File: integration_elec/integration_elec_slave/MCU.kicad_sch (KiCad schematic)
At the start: 0 parts

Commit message: EM - Ajout des pages hiérarchiques pour le slave, next up : Master
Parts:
- added C1, C2, C3, C4, C5, C6, C7, C8, C9: 0.10uF, Capacitor_SMD:C_0805_2012Metric_Pad1.18x1.45mm_HandSolder, symbol Device:C_Small
- added C10: 4.7uF, Capacitor_SMD:C_0805_2012Metric_Pad1.18x1.45mm_HandSolder, symbol Device:C_Small
- added C11, C12: 10pF, Capacitor_SMD:C_0805_2012Metric_Pad1.18x1.45mm_HandSolder, symbol Device:C_Small
- added L1: FerritBead 600 OHM, Inductor_SMD:L_0805_2012Metric_Pad1.15x1.40mm_HandSolder, symbol Device:FerriteBead
- added R2, R3, R38: 10k, Resistor_SMD:R_0805_2012Metric_Pad1.20x1.40mm_HandSolder, symbol Device:R_US
- added R37: 120, Resistor_SMD:R_0805_2012Metric_Pad1.20x1.40mm_HandSolder, symbol Device:R_US
- added SW1: SW_Push, Button_Switch_SMD:SW_SPST_TL3342, symbol Switch:SW_Push
- added U1: STM32F446RETx, Package_QFP:LQFP-64_10x10mm_P0.5mm, symbol MCU_ST_STM32F4:STM32F446RETx
- added Y1: Crystal_16MHz, ab2_xtal:CSM-3X, symbol Device:Crystal
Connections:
- new net: C6.2, L1.2, U1.13 (VDDA)
- new net: C10.2, C9.2, U1.30 (VCAP_1)
- new net: R3.2, U1.34 (PB13)
- new net: C11.1, U1.5 (PH0), Y1.1
- new net: C12.1, U1.6 (PH1), Y1.2
- new net: R2.1, U1.60 (BOOT0)
- new net: R37.1, SW1.1
- new net +3V3: C1.1, C2.1, C3.1, C4.1, C5.1, C7.1, L1.1, R38.1, U1.1 (VBAT), U1.19 (VDD), U1.32 (VDD), U1.48 (VDD), U1.64 (VDD)
- new net DEBUG_NJTRST: U1.56 (PB4)
- new net DEBUG_RESET: C8.1, R38.2, SW1.2, U1.7 (NRST)
- new net DEBUG_SWCLK_TCK: U1.49 (PA14)
- new net DEBUG_SWDIO_TMS: U1.46 (PA13)
- new net DEBUG_SWO_TDI: U1.50 (PA15)
- new net DEBUG_SWO_TDO: U1.55 (PB3)
- new net DEBUG_UART_RX: U1.25 (PC5)
- new net DEBUG_UART_TX: U1.29 (PB10)
- new net GND: C1.2, C10.1, C11.2, C12.2, C2.2, C3.2, C4.2, C5.2, C6.1, C7.2, C8.2, C9.1, R2.2, R37.2, U1.12 (VSSA), U1.18 (VSS), U1.31 (VSS), U1.47 (VSS), U1.63 (VSS)
- new net RF.XBEE_LED: U1.24 (PC4)
- new net RF.XBEE_RQ: U1.41 (PA8)
- new net RF.XBEE_STATUS: U1.40 (PC9)
- new net RF.XBEE_UART_CTS: U1.44 (PA11)
- new net RF.XBEE_UART_IN: U1.42 (PA9)
- new net RF.XBEE_UART_OUT: U1.43 (PA10)
- new net RF.XBEE_UART_RTS: U1.45 (PA12)
- new net RF.XBEE_nReset: U1.51 (PC10)
- new net SD_SDIO_CLK: U1.28 (PB2)
- new net SD_SDIO_CMD: U1.54 (PD2)
- new net SD_SDIO_D0: U1.39 (PC8)
- new net SD_SDIO_D1: U1.26 (PB0)
- new net SD_SDIO_D2: U1.27 (PB1)
- new net SD_SDIO_D3: U1.52 (PC11)
- new net SD_SDIO_SW: U1.53 (PC12)
- new net USB_D+: U1.36 (PB15)
- new net USB_D-: U1.35 (PB14)
- new net USB_ID: U1.33 (PB12)
- new net USB_VBUS: R3.1
- no-connect marks 0 -> 5
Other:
- note added: "If the flash is blank, the bootloader will enable."
- note added: "RESET"
- note added: "Stabilization for the main regulator"

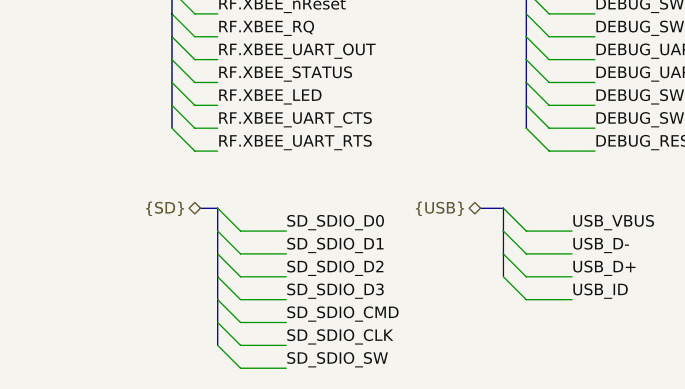
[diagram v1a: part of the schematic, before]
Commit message: EM - Avancement du slave et determination ADC pour LTF6800
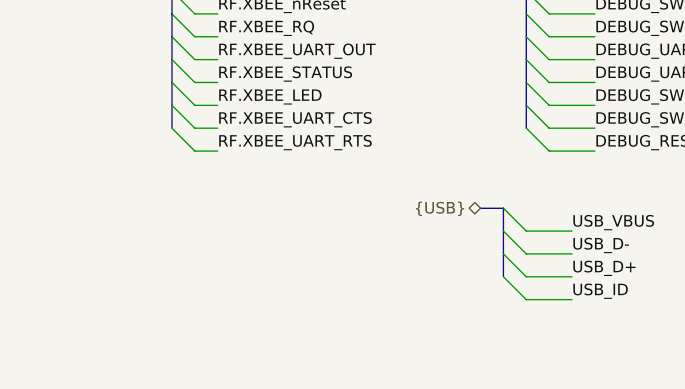
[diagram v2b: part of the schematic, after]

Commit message: EM - fuck it we merge et on cree deux branches
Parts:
- renumbered C1 to C11, C2 to C12, C3 to C13, C4 to C14, C5 to C15, C6 to C16, C7 to C17, C11 to C6, C8 to C7, C12 to C8, R37 to R5, R38 to R6, R2 to R7, R3 to R8, U1 to U2
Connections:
- net I2C_SCL: now reaches U2.58 (PB6)
- net I2C_SDA: now reaches U2.59 (PB7)
- net SD_SDIO_CLK: no longer names the net of U2.28 (PB2)
- net SD_SDIO_CMD: no longer names the net of U2.54 (PD2)
- net SD_SDIO_D0: no longer names the net of U2.39 (PC8)
- net SD_SDIO_D1: no longer names the net of U2.26 (PB0)
- net SD_SDIO_D2: no longer names the net of U2.27 (PB1)
- net SD_SDIO_D3: no longer names the net of U2.52 (PC11)
- net SD_SDIO_SW: no longer names the net of U2.53 (PC12)

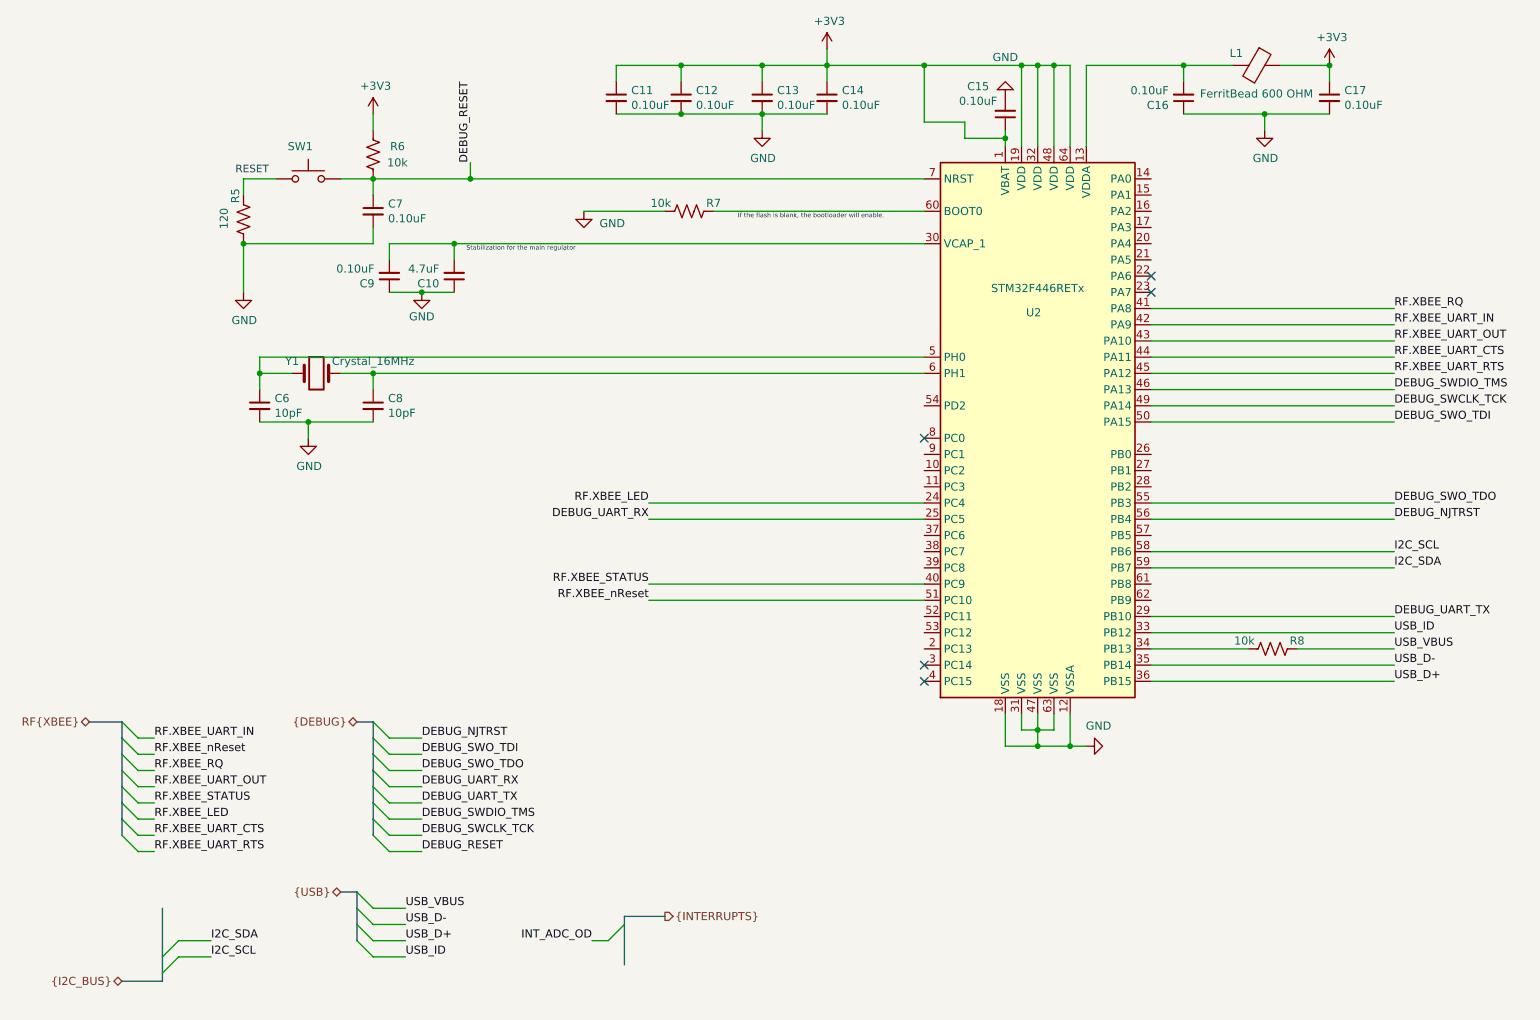
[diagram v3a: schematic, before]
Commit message: EM - Correction des bus
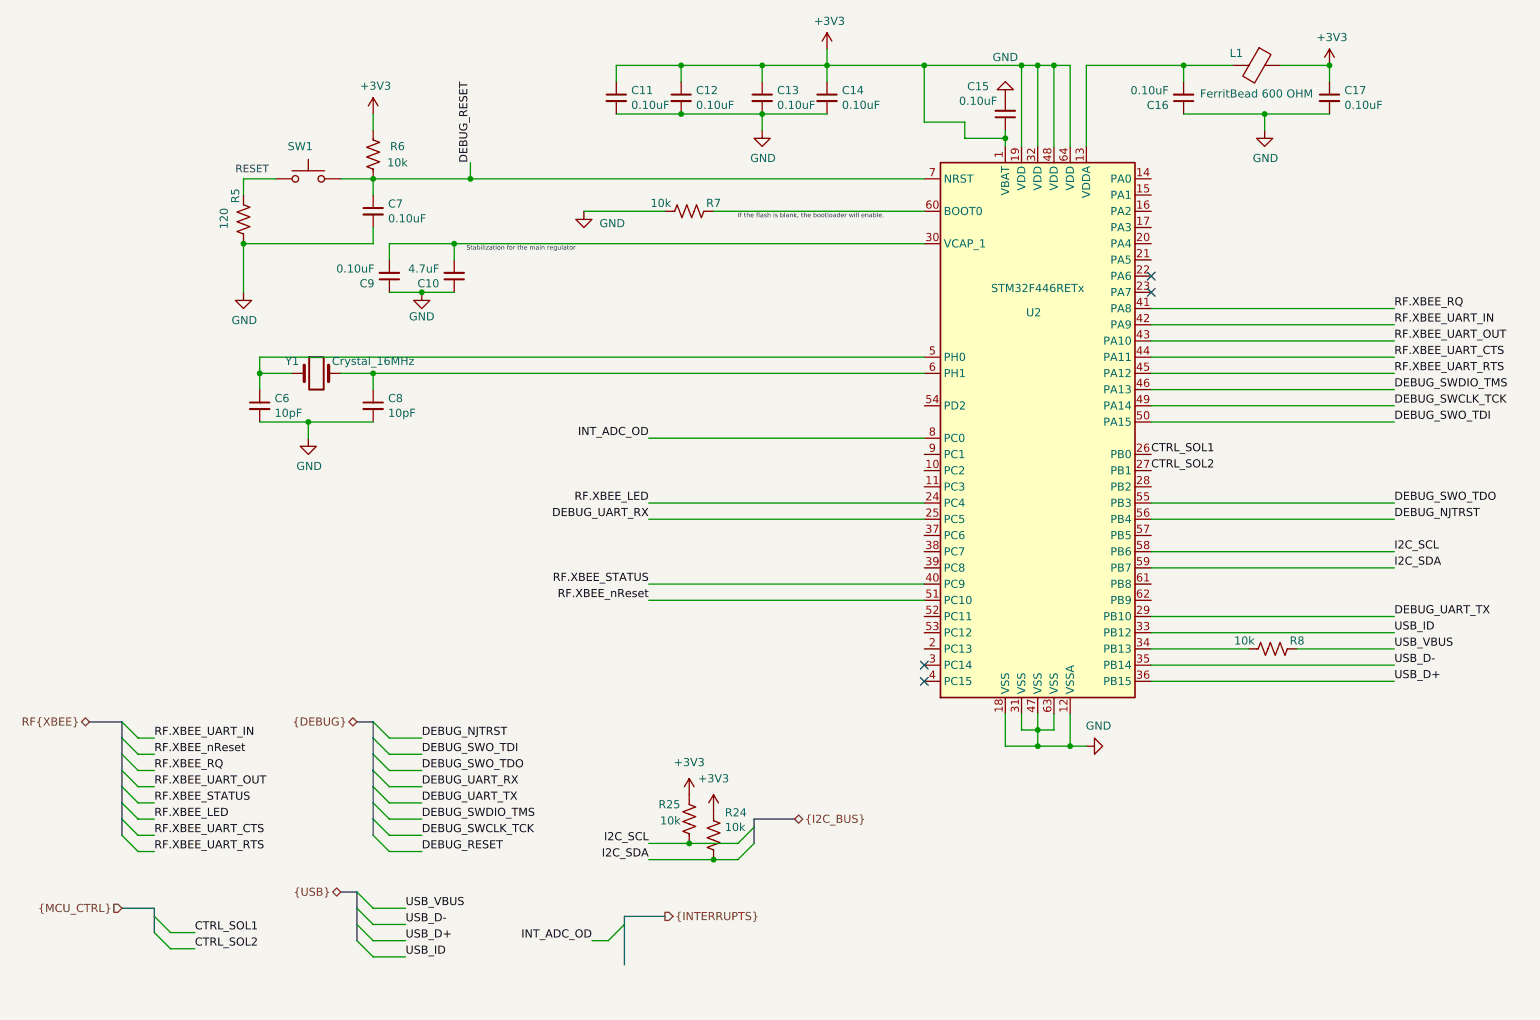
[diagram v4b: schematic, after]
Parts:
- added R24, R25: 10k, symbol Device:R_US
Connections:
- net +3V3: now also R24.1, R25.1
- net I2C_SCL: now also R25.2
- net I2C_SDA: now also R24.2
- net INT_ADC_OD: now also U2.8 (PC0)
- net CTRL_SOL1: now reaches U2.26 (PB0)
- net CTRL_SOL2: now reaches U2.27 (PB1)
- no-connect marks 5 -> 4

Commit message: EM - Fini schématique attente de review
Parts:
- R24, R25: footprint (none) -> Resistor_SMD:R_0805_2012Metric_Pad1.20x1.40mm_HandSolder; DigiKey (none) -> 311-10.0KCRCT-ND; Manufacturer (none) -> Yageo; Manufacturer Part Number (none) -> RC0805FR-0710KL

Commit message: EM - Review pas mal finale
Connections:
- no-connect marks 4 -> 24
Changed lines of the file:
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@@
+	)
+	(no_connect
+		(at 156.21 104.14)
+	)
+	(no_connect
+		(at 156.21 116.84)
+	)
+	(no_connect
+		(at 191.77 116.84)
+	)
+	(no_connect
+		(at 191.77 66.04)
+	)
+	(no_connect
+		(at 156.21 121.92)
+	)
+	(no_connect
+		(at 191.77 124.46)
+	)
+	(no_connect
+		(at 156.21 129.54)
+	)
+	(no_connect
+		(at 191.77 73.66)
+	)
+	(no_connect
+		(at 191.77 68.58)
 	)
 	(no_connect
@@
 	)
 	(no_connect
+		(at 156.21 132.08)
+	)
+	(no_connect
+		(at 156.21 109.22)
+	)
+	(no_connect
+		(at 156.21 106.68)
+	)
+	(no_connect
+		(at 191.77 127)
+	)
+	(no_connect
 		(at 191.77 78.74)
 	)
 	(no_connect
+		(at 191.77 109.22)
+	)
+	(no_connect
+		(at 191.77 60.96)
+	)
+	(no_connect
+		(at 156.21 119.38)
+	)
+	(no_connect
+		(at 156.21 96.52)
+	)
+	(no_connect
+		(at 191.77 63.5)
+	)
+	(no_connect
+		(at 191.77 71.12)
+	)
+	(no_connect
+		(at 156.21 134.62)
+	)
+	(no_connect
